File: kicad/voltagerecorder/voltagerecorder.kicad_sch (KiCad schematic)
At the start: 36 parts, among them J1 Conn_02x10_Odd_Even, J2 Phoenix Stecker, J3 Conn_01x08, U1 Opamp_Quad, U2 DCDC_BIPOLAR, U3 ADS8638, U4 Vreg_3pin, U5 Vreg_3pin

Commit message: Footprints komplett zugeordnet.
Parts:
- removed J3: Conn_01x08, symbol Connector_Generic:Conn_01x08
- removed U3: ADS8638, Package_DFN_QFN:QFN-24-1EP_4x4mm_P0.5mm_EP2.7x2.7mm, symbol cf:ADS8638
- removed U4: Vreg_3pin, Package_TO_SOT_SMD:SOT-89-3_Handsoldering, symbol cf:Vreg_3pin
- removed U5: Vreg_3pin, symbol cf:Vreg_3pin
- added C22: 3.3n, Capacitor_SMD:C_0603_1608Metric_Pad1.08x0.95mm_HandSolder, symbol Device:C
- added C24: 470u, Capacitor_SMD:CP_Elec_8x10.5, symbol Device:C_Polarized
- added C26, C28: 1u, Capacitor_SMD:C_0603_1608Metric_Pad1.08x0.95mm_HandSolder, symbol Device:C
- added J3: Conn_02x08_Odd_Even, Connector_PinHeader_2.54mm:PinHeader_2x08_P2.54mm_Vertical, symbol Connector_Generic:Conn_02x08_Odd_Even
- added R32, R33: nc, Resistor_SMD:R_0603_1608Metric_Pad0.98x0.95mm_HandSolder, symbol Device:R
- added U3: L78L12ACUTR, Package_TO_SOT_SMD:SOT-89-3_Handsoldering, symbol cf:L78L12ACUTR
- added U4: L79L12ACUTR, Package_TO_SOT_SMD:SOT-89-3_Handsoldering, symbol cf:L79L12ACUTR
- added U5: ADS8638, Package_DFN_QFN:QFN-24-1EP_4x4mm_P0.5mm_EP2.7x2.7mm, symbol cf:ADS8638
- C1: value 100n -> 1u; footprint (none) -> Capacitor_SMD:C_0603_1608Metric_Pad1.08x0.95mm_HandSolder
- C10, C12, C13, C14, C15, C16, C17, C18, C3, C6, C9: footprint (none) -> Capacitor_SMD:C_0603_1608Metric_Pad1.08x0.95mm_HandSolder
- C11, C2: value 100n -> 3.3n; footprint (none) -> Capacitor_SMD:C_0603_1608Metric_Pad1.08x0.95mm_HandSolder
- C19, C20, C5, C7, C8: footprint (none) -> Capacitor_SMD:CP_Elec_6.3x5.7
- C4: value 1u -> 3.3n; footprint (none) -> Capacitor_SMD:C_0603_1608Metric_Pad1.08x0.95mm_HandSolder
- J1: footprint (none) -> Connector_PinHeader_2.54mm:PinHeader_2x10_P2.54mm_Vertical
- J2: footprint (none) -> Connector_Phoenix_MC_HighVoltage:PhoenixContact_MC_1,5_5-G-5.08_1x05_P5.08mm_Horizontal
- JP1, JP2, JP3, JP4: footprint (none) -> Jumper:SolderJumper-3_P1.3mm_Open_RoundedPad1.0x1.5mm
- JP5: footprint (none) -> Jumper:SolderJumper-2_P1.3mm_Open_RoundedPad1.0x1.5mm
- R1, R2, R3: footprint (none) -> Resistor_SMD:R_0603_1608Metric_Pad0.98x0.95mm_HandSolder
- U2: footprint (none) -> cf:DCDC_BIPOLAR; MF (none) -> GAPTEC ELECTRONIC; MPN (none) -> 3S7B_0515D3U
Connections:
- net +12V: now also C26.1, R32.2, U3.1 (OUT), U5.14 (HVDD); no longer C3.1
- net +15V: now also U2.7 (VOUT+), R32.1, U3.3 (IN); no longer U2. (VOUT-)
- net +3.3V: now also J1.11 (Pin_11), C24.1, J3.11 (Pin_11), J3.12 (Pin_12), U5.21 (DVDD); no longer J1.17 (Pin_17)
- net +5V: now also J1.17 (Pin_17), U2.1 (VIN), J3.13 (Pin_13), J3.14 (Pin_14), U5.1 (AVDD); no longer U2. (VOUT-)
- net -12V: now also C3.2, C28.2, R33.2, U4.3 (OUT), U5.15 (HVSS); no longer C2.2, C4.2
- net -15V: now also U2.5 (VOUT-), R33.1, U4.2,4 (IN); no longer U2. (VOUT-)
- net AL_PD: now also U5.22 (AL_PD)
- net CS: now also J3.7 (Pin_7), J3.8 (Pin_8), U5.16 (CS)
- net GND: now also C2.2, C3.1, C4.2, U2.2 (GND_IN), U2.6 (GND_OUT), C22.2, C24.2, C26.2, C28.1, J3.15 (Pin_15), J3.16 (Pin_16), U3.2,4 (GND), U4.1 (GND), U5.2,3 (AGND), U5.20 (DGND), U5.23 (REFGND), U5.5 (AINGND); no longer C2.1, C3.2, C4.1, U2. (VOUT-)
- net IN0_EXT: now also U5.13 ((AIN0))
- net IN1_EXT: now also U5.12 ((AIN1))
- net IN6_EXT: now also U5.7 ((AIN6))
- net IN7_EXT: now also U5.6 ((AIN7))
- net MISO: now also J3.5 (Pin_5), J3.6 (Pin_6)
- net MOSI: now also J3.3 (Pin_3), J3.4 (Pin_4), U5.18 (DIN)
- net PD: now also J3.10 (Pin_10), J3.9 (Pin_9)
- net REF_EXT: now also J1.12 (Pin_12); no longer J1.10 (Pin_10)
- net SCLK: now also J3.1 (Pin_1), J3.2 (Pin_2), U5.17 (SCLK)
- net at C14.1, JP5.1 (A): now also U5.24 (REF); no longer C11.1
- net at JP4.2 (C): now also C22.1, U5.8 (AIN5)
- net at JP1.2 (C): now also C2.1, U5.11 (AIN2)
- net at JP2.2 (C): now also C4.1, U5.10 (AIN3)
- net at R1.1: now also U5.19 (DOUT)
- net at JP3.2 (C): now also C11.1, U5.9 (AIN4)
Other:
- note added: "3W: max. 47uF alle anderen: max. 220uF"
- note added: "C0G"
- note added: "Es gibt 2 Gehäusestandards, äußerer Pinabstand 15.24mm (3kV Isolation) oder 12.7mm (1.5kV Isolation). Den mit 15.24 nehmen, er ist universeller und es gibt Module bis 3W. 1W, ca. 2,80€: CUI PEME1-S5-D5-S 3W, ca. 6,50€: Gaptec 3S7B_0515D3U"
- note removed: "z.B. Traco TBA 2-0523 5V in, +-15V out, 2W (=65mA) 4.50€ bei 1 Stk."
- moved on the sheet: C10, C12, C13, C14, C15, C16, C17, C18, C19, C20, C3, C5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

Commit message: a
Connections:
- net -15V: now also U4.2 (IN); no longer U4.2,4 (IN)
- net GND: now also U3.2 (GND), U5.2 (AGND), U5.25 (PLANE), U5.3 (AGND2); no longer U3.2,4 (GND), U5.2,3 (AGND)
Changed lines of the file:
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@@
+    (stroke (width 0) (type default) (color 0 0 0 0))
+  )
+  (wire (pts (xy 160.02 83.82) (xy 160.02 81.28))
     (stroke (width 0) (type default) (color 0 0 0 0))
   )
@@
     (stroke (width 0) (type default) (color 0 0 0 0))
   )
+  (wire (pts (xy 130.81 93.98) (xy 134.62 93.98))
+    (stroke (width 0) (type default) (color 0 0 0 0))
+  )
   (wire (pts (xy 40.64 63.5) (xy 48.26 63.5))
     (stroke (width 0) (type default) (color 0 0 0 0))
@@
   )
   (wire (pts (xy 160.02 60.96) (xy 171.45 60.96))
+    (stroke (width 0) (type default) (color 0 0 0 0))
+  )
+  (wire (pts (xy 157.48 83.82) (xy 160.02 83.82))
     (stroke (width 0) (type default) (color 0 0 0 0))
   )
@@
     )
     (property "Datasheet" "" (id 3) (at 46.99 125.73 0)
+      (effects (font (size 1.27 1.27)) hide)
+    )
+    (pin "1")
+  )
+  (symbol (lib_id "power:GND") (at 130.81 93.98 270) (unit 1)
+    (in_bom yes) (on_board yes)
+    (property "Reference" "#PWR?" (id 0) (at 124.46 93.98 0)
+      (effects (font (size 1.27 1.27)) hide)
+    )
+    (property "Value" "GND" (id 1) (at 127 92.71 0)
+      (effects (font (size 1.27 1.27)) (justify left))
+    )
+    (property "Footprint" "" (id 2) (at 130.81 93.98 0)
+      (effects (font (size 1.27 1.27)) hide)
+    )
+    (property "Datasheet" "" (id 3) (at 130.81 93.98 0)
       (effects (font (size 1.27 1.27)) hide)
     )
@@
     (pin "18")
     (pin "19")
-    (pin "2,3")
+    (pin "2")
     (pin "20")
     (pin "21")
@@
     (pin "23")
     (pin "24")
+    (pin "25")
+    (pin "3")
     (pin "5")
     (pin "6")
@@
     )
     (pin "1")
-    (pin "2,4")
+    (pin "2")
     (pin "3")
   )
@@
     )
     (pin "1")
-    (pin "2,4")
+    (pin "2")
     (pin "3")
   )
@@
       (reference "#PWR0110") (unit 1) (value "GND") (footprint "")
     )
+    (path "/5f81148b-c354-4d3b-a06a-bfedff63f746"
+      (reference "#PWR?") (unit 1) (value "GND") (footprint "")
+    )
     (path "/daf84f24-8dd6-4544-a1d3-e83433eceeb9"

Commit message: placing finished
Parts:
- removed J3: Conn_02x08_Odd_Even, Connector_PinHeader_2.54mm:PinHeader_2x08_P2.54mm_Vertical, symbol Connector_Generic:Conn_02x08_Odd_Even
- removed R32, R33: nc, Resistor_SMD:R_0603_1608Metric_Pad0.98x0.95mm_HandSolder, symbol Device:R
- added J3: Conn_01x08, Connector_PinHeader_2.54mm:PinHeader_1x08_P2.54mm_Vertical, symbol Connector_Generic:Conn_01x08
- C14: footprint Capacitor_SMD:C_0603_1608Metric_Pad1.08x0.95mm_HandSolder -> Capacitor_SMD:C_0805_2012Metric_Pad1.18x1.45mm_HandSolder
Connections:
- net +3.3V: now also J3.6 (Pin_6)
- net +5V: now also J3.7 (Pin_7)
- net CS: now also J3.4 (Pin_4)
- net GND: now also J3.8 (Pin_8)
- net MISO: now also J3.3 (Pin_3)
- net MOSI: now also J3.2 (Pin_2)
- net PD: now also J3.5 (Pin_5)
- net SCLK: now also J3.1 (Pin_1)
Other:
- moved on the sheet: C17, C18, C19, C20, U3, U4

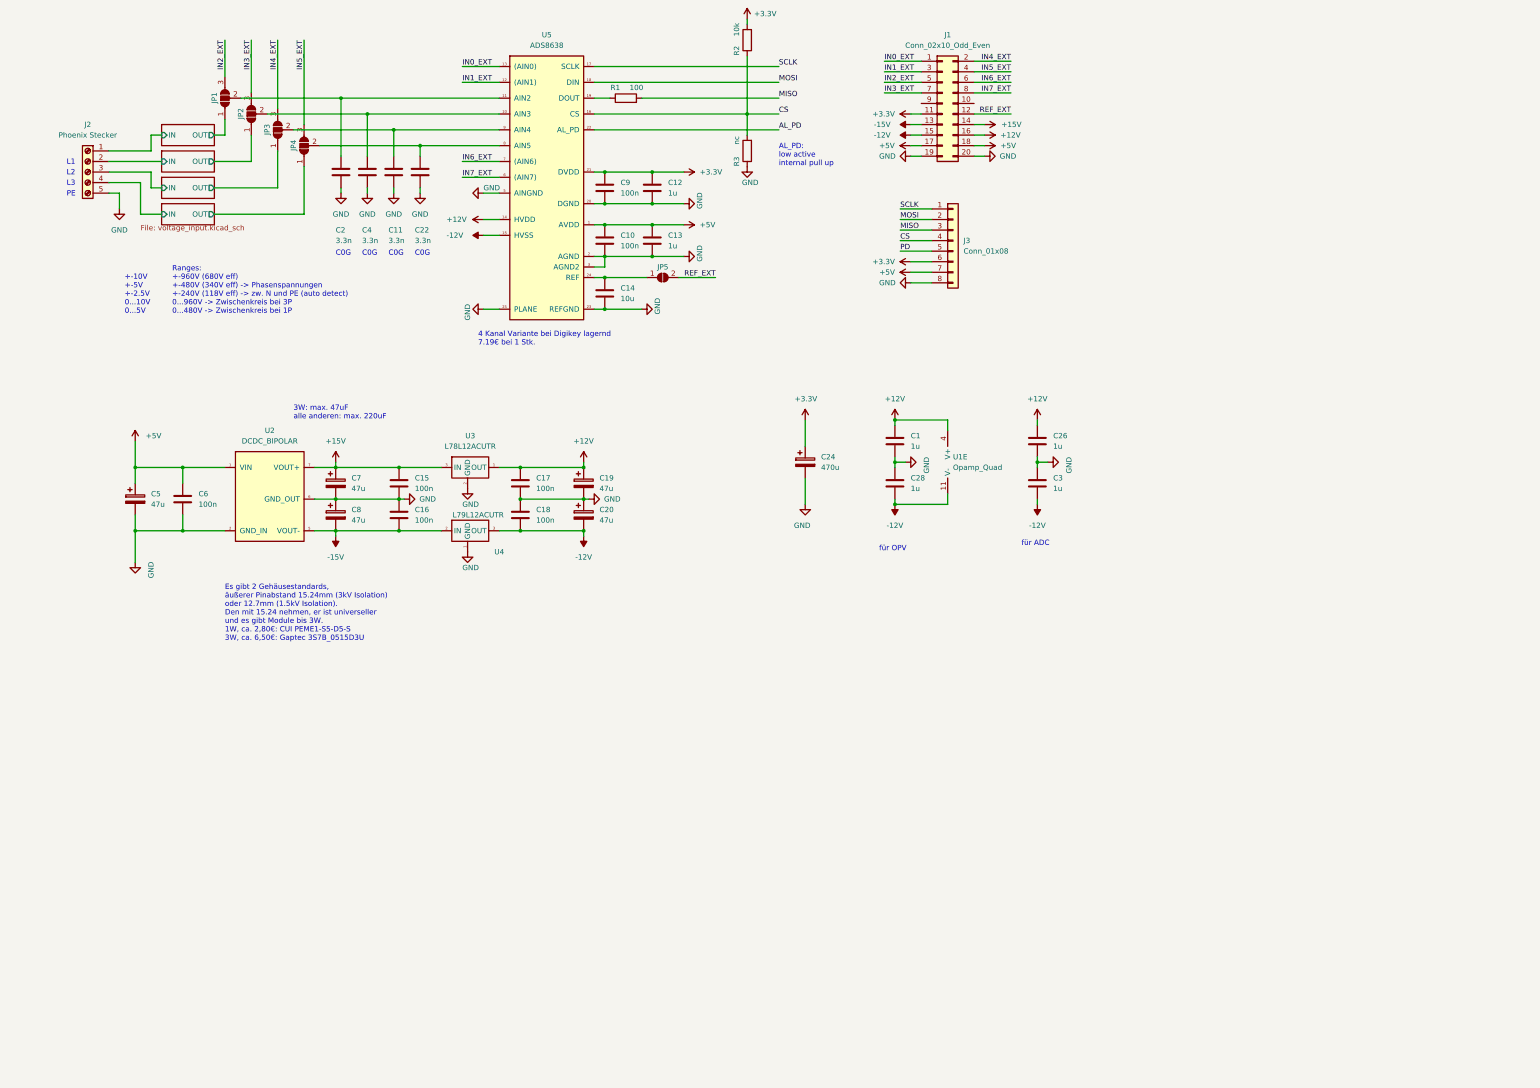
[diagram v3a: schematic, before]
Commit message: ESP32-S3 WROOM 2 hinzugefügt.
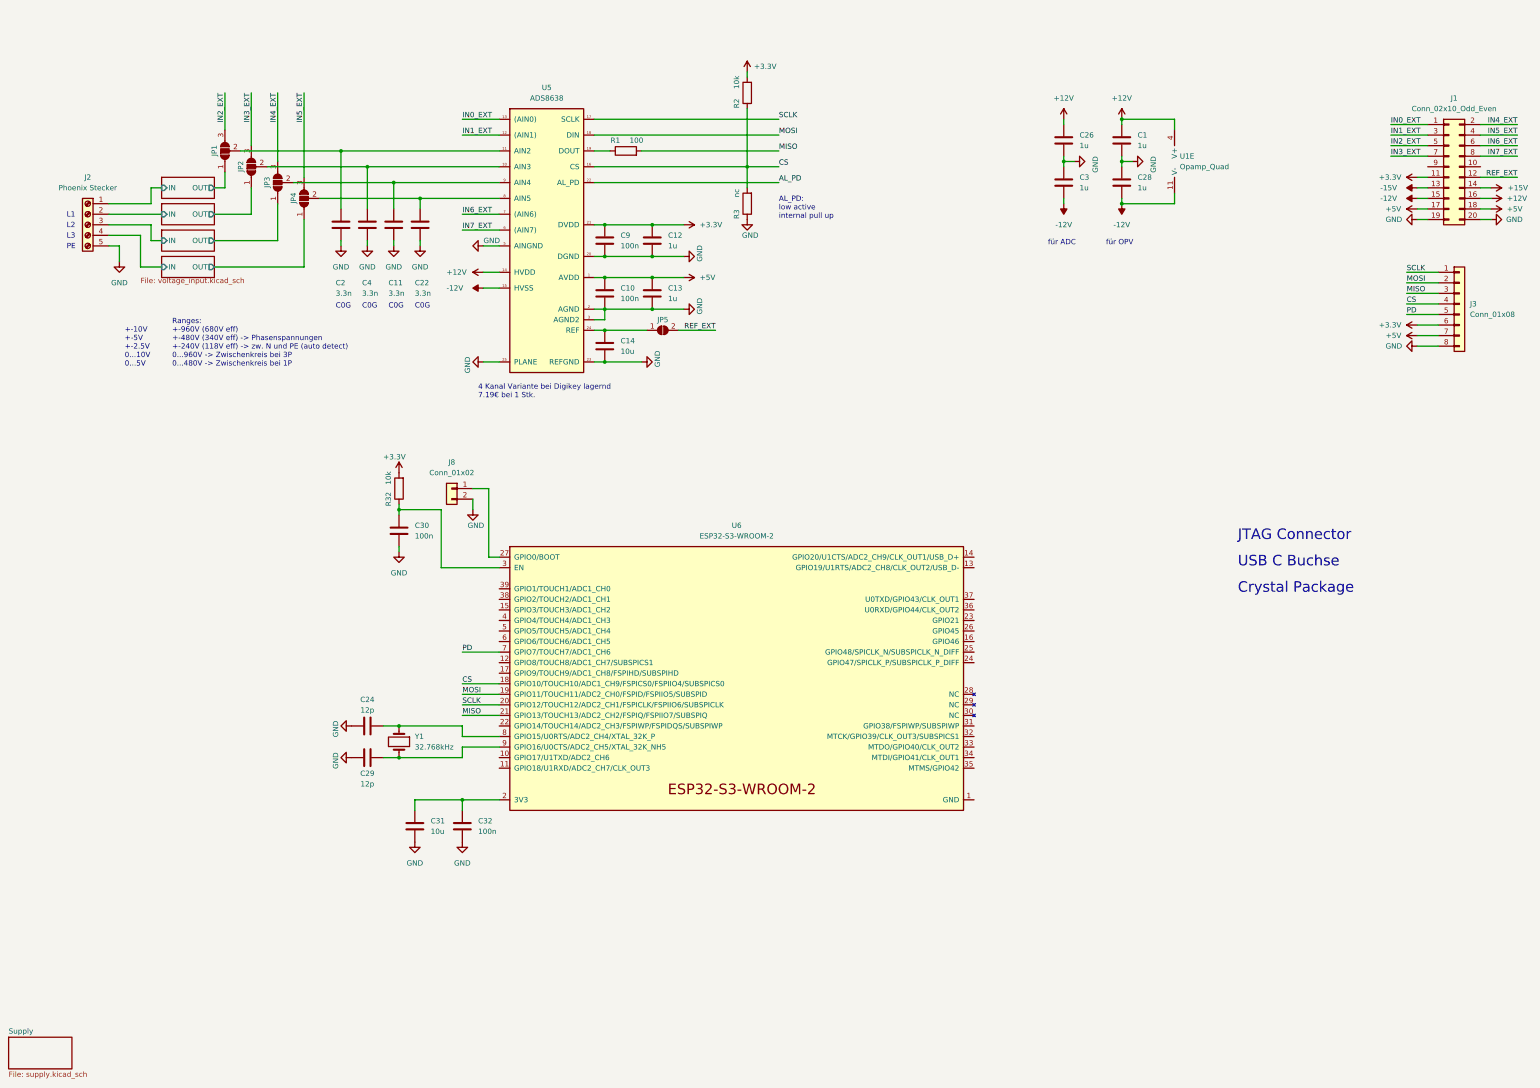
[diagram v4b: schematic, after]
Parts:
- removed C15, C16, C17, C18, C6: 100n, Capacitor_SMD:C_0603_1608Metric_Pad1.08x0.95mm_HandSolder, symbol Device:C
- removed C19, C20, C5, C7, C8: 47u, Capacitor_SMD:CP_Elec_6.3x5.7, symbol Device:C_Polarized
- removed C24: 470u, Capacitor_SMD:CP_Elec_8x10.5, symbol Device:C_Polarized
- removed U2: DCDC_BIPOLAR, cf:DCDC_BIPOLAR, symbol cf:DCDC_BIPOLAR
- removed U3: L78L12ACUTR, Package_TO_SOT_SMD:SOT-89-3_Handsoldering, symbol cf:L78L12ACUTR
- removed U4: L79L12ACUTR, Package_TO_SOT_SMD:SOT-89-3_Handsoldering, symbol cf:L79L12ACUTR
- added C24, C29: 12p, Capacitor_SMD:C_0603_1608Metric_Pad1.08x0.95mm_HandSolder, symbol Device:C
- added C30, C32: 100n, Capacitor_SMD:C_0603_1608Metric_Pad1.08x0.95mm_HandSolder, symbol Device:C
- added C31: 10u, Capacitor_SMD:C_0805_2012Metric_Pad1.18x1.45mm_HandSolder, symbol Device:C
- added J8: Conn_01x02, Connector_PinHeader_2.54mm:PinHeader_1x02_P2.54mm_Vertical, symbol Connector_Generic:Conn_01x02
- added R32: 10k, Resistor_SMD:R_0603_1608Metric_Pad0.98x0.95mm_HandSolder, symbol Device:R
- added U6: ESP32-S3-WROOM-2, Espressif:ESP32-S3-WROOM-2, symbol espressif:ESP32-S3-WROOM-2
- added Y1: 32.768kHz, Crystal:Crystal_SMD_SeikoEpson_MC306-4Pin_8.0x3.2mm_HandSoldering, symbol Device:Crystal
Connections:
- net +3.3V: now also R32.2
- net CS: now also U6.18 (GPIO10/TOUCH10/ADC1_CH9/FSPICS0/FSPIIO4/SUBSPICS0)
- net GND: now also C24.2, C29.2, C30.2, C31.2, C32.2, J8.2 (Pin_2)
- net MISO: now also U6.21 (GPIO13/TOUCH13/ADC2_CH2/FSPIQ/FSPIIO7/SUBSPIQ)
- net MOSI: now also U6.19 (GPIO11/TOUCH11/ADC2_CH0/FSPID/FSPIIO5/SUBSPID)
- net PD: now also U6.7 (GPIO7/TOUCH7/ADC1_CH6)
- net SCLK: now also U6.20 (GPIO12/TOUCH12/ADC2_CH1/FSPICLK/FSPIIO6/SUBSPICLK)
- new net: J8.1 (Pin_1), U6.27 (GPIO0/BOOT)
- new net: C30.1, R32.1, U6.3 (EN)
- new net: C31.1, C32.1, U6.2 (3V3)
- new net: C24.1, U6.8 (GPIO15/U0RTS/ADC2_CH4/XTAL_32K_P), Y1.1
- new net: C29.1, U6.9 (GPIO16/U0CTS/ADC2_CH5/XTAL_32K_NH5), Y1.2
- new net: U6.1 (GND), U6.40 (GND), U6.41 (GND)
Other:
- added sheet Supply (supply.kicad_sch)
- note added: "Crystal Package"
- note added: "JTAG Connector"
- note added: "USB C Buchse"
- note removed: "3W: max. 47uF alle anderen: max. 220uF"
- note removed: "Es gibt 2 Gehäusestandards, äußerer Pinabstand 15.24mm (3kV Isolation) oder 12.7mm (1.5kV Isolation). Den mit 15.24 nehmen, er ist universeller und es gibt Module bis 3W. 1W, ca. 2,80€: CUI PEME1-S5-D5-S 3W, ca. 6,50€: Gaptec 3S7B_0515D3U"
- moved on the sheet: C1, C10, C11, C12, C13, C14, C2, C22, C26, C28, C3, C4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
